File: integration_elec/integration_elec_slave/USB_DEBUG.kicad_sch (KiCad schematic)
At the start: 10 parts, among them J2 USB_C_Receptacle_USB2.0_16P, J5 CONN_02X05, U3 USBLC6-2SC6

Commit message: EM - fuck it we merge et on cree deux branches
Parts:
- renumbered J5 to J1, R1 to R10, R8 to R11, R175 to R12, R6 to R13, R7 to R9
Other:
- moved on the sheet: J1
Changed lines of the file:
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@@
 	(paper "A4")
 	(rectangle
-		(start 18.415 36.195)
-		(end 69.85 60.325)
+		(start 14.605 135.255)
+		(end 66.04 159.385)
 		(stroke
 			(width 0)
@@
 	)
 	(label "DEBUG_UART_TX"
-		(at 36.83 55.88 180)
+		(at 33.02 154.94 180)
 		(effects
 			(font
@@
 	)
 	(label "DEBUG_RESET"
-		(at 49.53 53.34 0)
+		(at 45.72 152.4 0)
 		(effects
 			(font
@@
 	)
 	(label "DEBUG_SWO_TDO"
-		(at 36.83 50.8 180)
+		(at 33.02 149.86 180)
 		(effects
 			(font
@@
 	)
 	(label "DEBUG_SWDIO_TMS"
-		(at 49.53 50.8 0)
+		(at 45.72 149.86 0)
 		(effects
 			(font
@@
 	)
 	(label "DEBUG_SWCLK_TCK"
-		(at 49.53 45.72 0)
+		(at 45.72 144.78 0)
 		(effects
 			(font
@@
 	)
 	(label "DEBUG_SWO_TDI"
-		(at 36.83 48.26 180)
+		(at 33.02 147.32 180)
 		(effects
 			(font
@@
 	)
 	(label "DEBUG_UART_RX"
-		(at 36.83 53.34 180)
+		(at 33.02 152.4 180)
 		(effects
 			(font
@@
 	)
 	(label "DEBUG_NJTRST"
-		(at 36.83 45.72 180)
+		(at 33.02 144.78 180)
 		(effects
 			(font
@@
 		(on_board yes)
 		(dnp no)
-		(property "Reference" "R7"
+		(property "Reference" "R9"
 			(at 156.845 66.04 90)
 			(effects
@@
 			(project "integration_elec_slave"
 				(path "/f8f45849-17b1-4cdb-b0ac-47b1208e44f3/e4c44223-4b52-473c-9d8d-296e2e6301bc"
-					(reference "R7")
+					(reference "R9")
 					(unit 1)
 				)
@@
 		(on_board yes)
 		(dnp no)
-		(property "Reference" "R6"
+		(property "Reference" "R13"
 			(at 254 68.58 0)
 			(effects
@@
 			(project "integration_elec_slave"
 				(path "/f8f45849-17b1-4cdb-b0ac-47b1208e44f3/e4c44223-4b52-473c-9d8d-296e2e6301bc"
-					(reference "R6")
+					(reference "R13")
 					(unit 1)
 				)
@@
 		(on_board yes)
 		(dnp no)
-		(property "Reference" "#PWR183"
+		(property "Reference" "#PWR026"
 			(at 229.87 49.53 0)
 			(effects
@@
 			(project "integration_elec_slave"
 				(path "/f8f45849-17b1-4cdb-b0ac-47b1208e44f3/e4c44223-4b52-473c-9d8d-296e2e6301bc"
-					(reference "#PWR183")
+					(reference "#PWR026")
 					(unit 1)
 				)
@@
 	(symbol
 		(lib_id "power:GND")
-		(at 49.53 48.26 90)
+		(at 45.72 147.32 90)
 		(unit 1)
 		(exclude_from_sim no)
@@
 		(on_board yes)
 		(dnp no)
-		(property "Reference" "#PWR038"
-			(at 55.88 48.26 0)
+		(property "Reference" "#PWR021"
+			(at 52.07 147.32 0)
 			(effects
 				(font
@@
 		)
 		(property "Value" "GND"
-			(at 54.864 48.26 90)
+			(at 51.054 147.32 90)
 			(effects
 				(font
@@
 		)
 		(property "Footprint" ""
-			(at 49.53 48.26 0)
+			(at 45.72 147.32 0)
 			(effects
 				(font
@@
 		)
 		(property "Datasheet" ""
-			(at 49.53 48.26 0)
+			(at 45.72 147.32 0)
 			(effects
 				(font
@@
 		)
 		(property "Description" ""
-			(at 49.53 48.26 0)
+			(at 45.72 147.32 0)
 			(effects
 				(font
@@
 			(project "integration_elec_slave"
 				(path "/f8f45849-17b1-4cdb-b0ac-47b1208e44f3/e4c44223-4b52-473c-9d8d-296e2e6301bc"
-					(reference "#PWR038")
+					(reference "#PWR021")
 					(unit 1)
 				)
@@
 		(on_board yes)
 		(dnp no)
-		(property "Reference" "R175"
+		(property "Reference" "R12"
 			(at 228.092 36.83 0)
 			(effects
@@
 			(project "integration_elec_slave"
 				(path "/f8f45849-17b1-4cdb-b0ac-47b1208e44f3/e4c44223-4b52-473c-9d8d-296e2e6301bc"
-					(reference "R175")
+					(reference "R12")
 					(unit 1)
 				)
@@
 	(symbol
 		(lib_id "power:+3V3")
-		(at 49.53 55.88 270)
+		(at 45.72 154.94 270)
 		(unit 1)
 		(exclude_from_sim no)
@@
 		(on_board yes)
 		(dnp no)
-		(property "Reference" "#PWR039"
-			(at 45.72 55.88 0)
+		(property "Reference" "#PWR022"
+			(at 41.91 154.94 0)
 			(effects
 				(font
@@
 		)
 		(property "Value" "+3V3"
-			(at 53.9242 56.261 0)
+			(at 50.1142 155.321 0)
 			(effects
 				(font
@@
 		)
 		(property "Footprint" ""
-			(at 49.53 55.88 0)
+			(at 45.72 154.94 0)
 			(effects
 				(font
@@
 		)
 		(property "Datasheet" ""
-			(at 49.53 55.88 0)
+			(at 45.72 154.94 0)
 			(effects
 				(font
@@
 		)
 		(property "Description" ""
-			(at 49.53 55.88 0)
+			(at 45.72 154.94 0)
 			(effects
 				(font
@@
 			(project "integration_elec_slave"
 				(path "/f8f45849-17b1-4cdb-b0ac-47b1208e44f3/e4c44223-4b52-473c-9d8d-296e2e6301bc"
-					(reference "#PWR039")
+					(reference "#PWR022")
 					(unit 1)
 				)
@@
 		(on_board yes)
 		(dnp no)
-		(property "Reference" "#PWR185"
+		(property "Reference" "#PWR025"
 			(at 222.25 49.53 0)
 			(effects
@@
 			(project "integration_elec_slave"
 				(path "/f8f45849-17b1-4cdb-b0ac-47b1208e44f3/e4c44223-4b52-473c-9d8d-296e2e6301bc"
-					(reference "#PWR185")
+					(reference "#PWR025")
 					(unit 1)
 				)
@@
 		(on_board yes)
 		(dnp no)
-		(property "Reference" "R8"
+		(property "Reference" "R11"
 			(at 220.472 36.83 0)
 			(effects
@@
 			(project "integration_elec_slave"
 				(path "/f8f45849-17b1-4cdb-b0ac-47b1208e44f3/e4c44223-4b52-473c-9d8d-296e2e6301bc"
-					(reference "R8")
+					(reference "R11")
 					(unit 1)
 				)
@@
 		(on_board yes)
 		(dnp no)
-		(property "Reference" "#PWR17"
+		(property "Reference" "#PWR027"
 			(at 250.19 82.55 0)
 			(effects
@@
 			(project "integration_elec_slave"
 				(path "/f8f45849-17b1-4cdb-b0ac-47b1208e44f3/e4c44223-4b52-473c-9d8d-296e2e6301bc"
-					(reference "#PWR17")
+					(reference "#PWR027")
 					(unit 1)
 				)
@@
 		(on_board yes)
 		(dnp no)
-		(property "Reference" "#PWR11"
+		(property "Reference" "#PWR023"
 			(at 187.96 60.96 0)
 			(effects
@@
 			(project "integration_elec_slave"
 				(path "/f8f45849-17b1-4cdb-b0ac-47b1208e44f3/e4c44223-4b52-473c-9d8d-296e2e6301bc"
-					(reference "#PWR11")
+					(reference "#PWR023")
 					(unit 1)
 				)
@@
 		(on_board yes)
 		(dnp no)
-		(property "Reference" "R1"
+		(property "Reference" "R10"
 			(at 164.465 35.56 90)
 			(effects
@@
 			(project "integration_elec_slave"
 				(path "/f8f45849-17b1-4cdb-b0ac-47b1208e44f3/e4c44223-4b52-473c-9d8d-296e2e6301bc"
-					(reference "R1")
+					(reference "R10")
 					(unit 1)
 				)
@@
 	(symbol
 		(lib_id "Connectors:CONN_02X05")
-		(at 43.18 50.8 0)
+		(at 39.37 149.86 0)
 		(unit 1)
 		(exclude_from_sim no)
@@
 		(dnp no)
 		(fields_autoplaced yes)
-		(property "Reference" "J5"
-			(at 43.18 39.878 0)
+		(property "Reference" "J1"
+			(at 39.37 138.938 0)
 			(effects
 				(font
@@
 		)
 		(property "Value" "CONN_02X05"
-			(at 43.18 42.418 0)
+			(at 39.37 141.478 0)
 			(effects
 				(font
@@
 		)
 		(property "Footprint" "Esteban11:CONN_CNC_10_pins"
-			(at 43.18 81.28 0)
+			(at 39.37 180.34 0)
 			(effects
 				(font
@@
 		)
 		(property "Datasheet" "http://www.cnctech.us/pdfs/3220-XX-0100-00_.pdf"
-			(at 43.18 81.28 0)
+			(at 39.37 180.34 0)
 			(effects
 				(font
@@
 		)
 		(property "Description" ""
-			(at 43.18 50.8 0)
+			(at 39.37 149.86 0)
 			(effects
 				(font
@@
 		)
 		(property "DigiKey" "1175-1627-ND"
-			(at 43.18 50.8 0)
+			(at 39.37 149.86 0)
 			(effects
 				(font
@@
 		)
 		(property "Manufacturer" "CNC tech"
-			(at 43.18 50.8 0)
+			(at 39.37 149.86 0)
 			(effects
 				(font
@@
 			(project "integration_elec_slave"
 				(path "/f8f45849-17b1-4cdb-b0ac-47b1208e44f3/e4c44223-4b52-473c-9d8d-296e2e6301bc"
-					(reference "J5")
+					(reference "J1")
 					(unit 1)
 				)
@@
 		(on_board yes)
 		(dnp no)
-		(property "Reference" "#PWR9"
+		(property "Reference" "#PWR024"
 			(at 200.66 39.37 0)
 			(effects
@@
 			(project "integration_elec_slave"
 				(path "/f8f45849-17b1-4cdb-b0ac-47b1208e44f3/e4c44223-4b52-473c-9d8d-296e2e6301bc"
-					(reference "#PWR9")
+					(reference "#PWR024")
 					(unit 1)
 				)

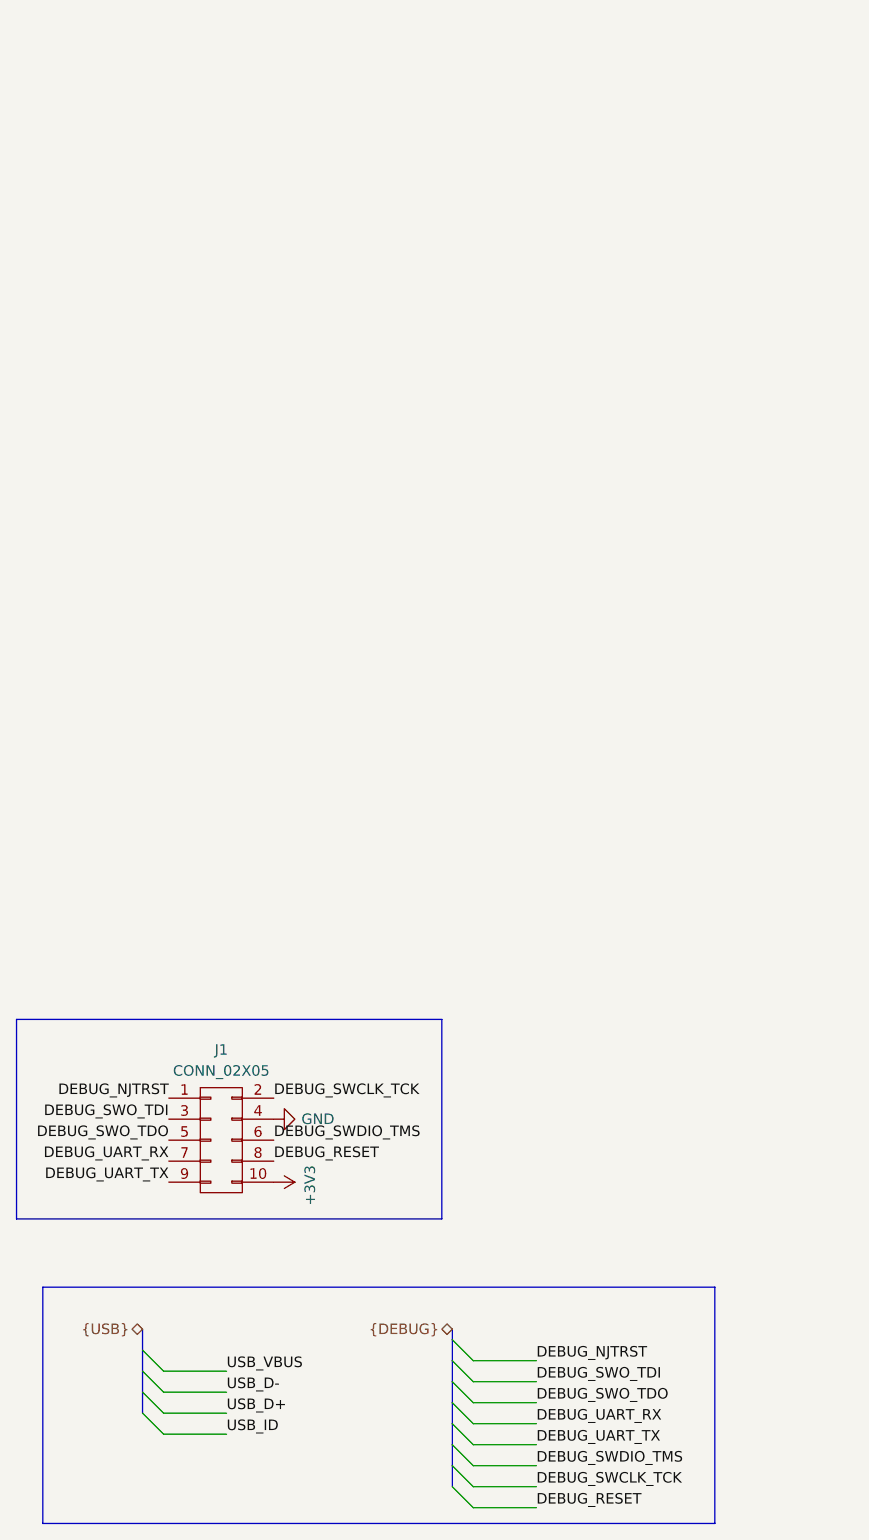
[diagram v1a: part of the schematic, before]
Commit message: EM - Correction des bus
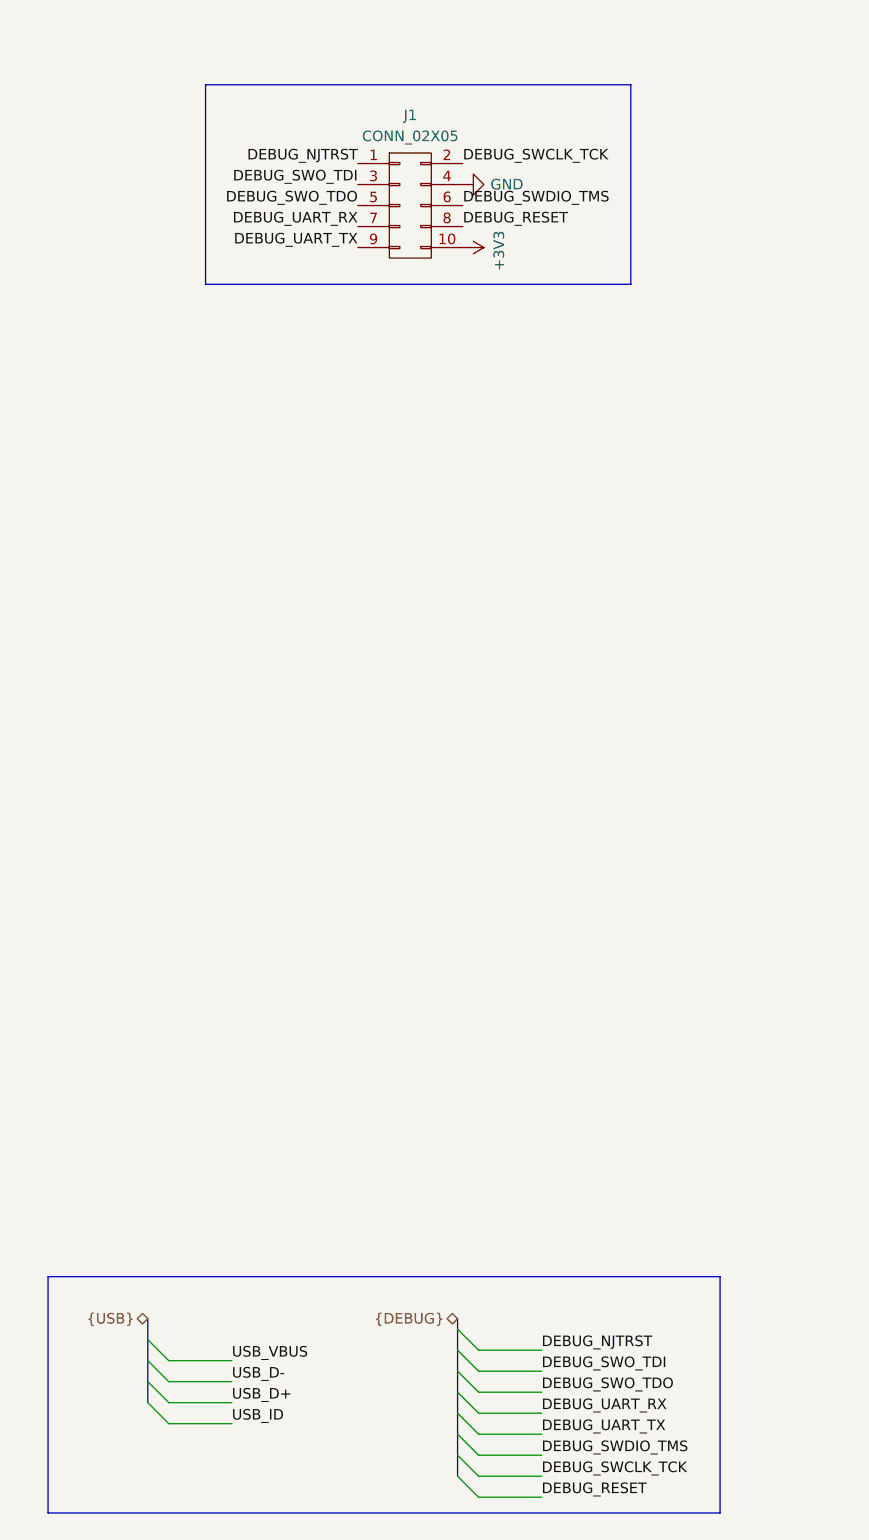
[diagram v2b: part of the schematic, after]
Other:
- moved on the sheet: J1

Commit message: EM - Fini schématique attente de review
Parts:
- J2: DigiKey (none) -> 2073-USB4105-GF-ACT-ND
- R11, R12: DigiKey (none) -> 311-5.10KHRCT-ND
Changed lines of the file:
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@@
+			)
+		)
+		(property "DigiKey" "2073-USB4105-GF-ACT-ND"
+			(at 250.19 40.64 0)
+			(effects
+				(font
+					(size 1.27 1.27)
+				)
+				(hide yes)
 			)
 		)
@@
 			)
 		)
+		(property "DigiKey" "311-5.10KHRCT-ND"
+			(at 229.87 38.1 0)
+			(effects
+				(font
+					(size 1.27 1.27)
+				)
+				(hide yes)
+			)
+		)
 		(pin "1"
 		)
@@
 			(at 222.25 38.1 0)
 			(effects
+				(font
+					(size 1.27 1.27)
+				)
+				(hide yes)
+			)
+		)
+		(property "DigiKey" "311-5.10KHRCT-ND"
+			(at 222.25 38.1 0)
+			(effects
